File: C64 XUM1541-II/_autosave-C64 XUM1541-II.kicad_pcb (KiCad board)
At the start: 2 copper layers, 64.1 x 39.4 mm, 18 parts, among them J1 C64_IEC, J2 SpeedDOS, M1 Mounting, M2 Mounting, M3 Mounting, M4 Mounting, SW1 RESET, U1 7406

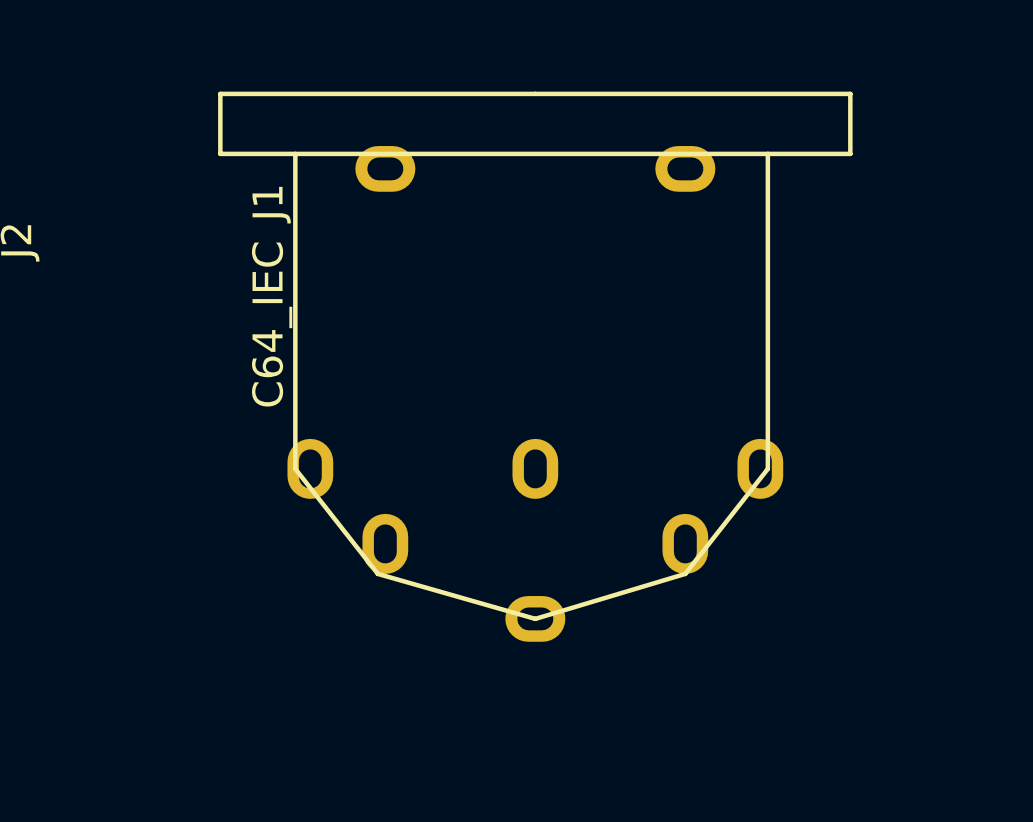
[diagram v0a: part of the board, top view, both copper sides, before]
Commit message: User port adapter added
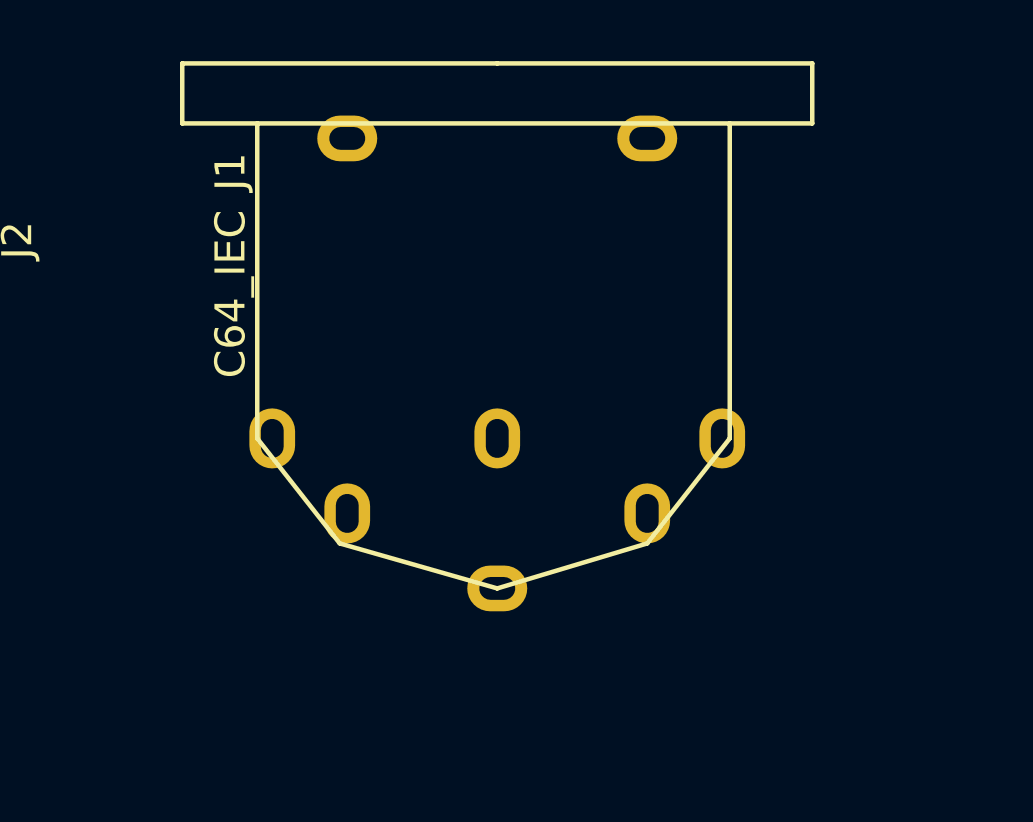
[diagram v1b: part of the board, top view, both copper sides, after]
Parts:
- moved J1 1.63 mm to (115.3, 45.7)
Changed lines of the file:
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@@
   )
   (module C64_IEC:C64_IEC (layer F.Cu)
-    (at 116.586 46.736 180)
+    (at 115.316 45.72 180)
     (fp_text reference J1 (at 8.89 8.89 270) (layer F.SilkS)
       (effects (font (size 1 1) (thickness 0.15)))
